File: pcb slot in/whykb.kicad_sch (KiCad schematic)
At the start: 89 parts, among them K1 KEYSW, K10 KEYSW, K11 KEYSW, K12 KEYSW, K13 KEYSW, K14 KEYSW, K15 KEYSW, K16 KEYSW, K17 KEYSW, K18 KEYSW, K19 KEYSW, K2 KEYSW, K20 KEYSW, K21 KEYSW, K22 KEYSW, K23 KEYSW, K24 KEYSW, K25 KEYSW, K26 KEYSW, K27 KEYSW, K28 KEYSW, K29 KEYSW, K3 KEYSW, K30 KEYSW, K31 KEYSW, K32 KEYSW, K33 KEYSW, K34 KEYSW, K35 KEYSW, K36 KEYSW, K37 KEYSW, K38 KEYSW, K39 KEYSW, K4 KEYSW, K40 KEYSW, K41 KEYSW, K42 KEYSW, K5 KEYSW, K6 KEYSW, K7 KEYSW, K8 KEYSW, K9 KEYSW, SW1 SW_PUSH, SW2 RotaryEncoder_Switch, U1 Elite-C, U2 SSD1306 128x32

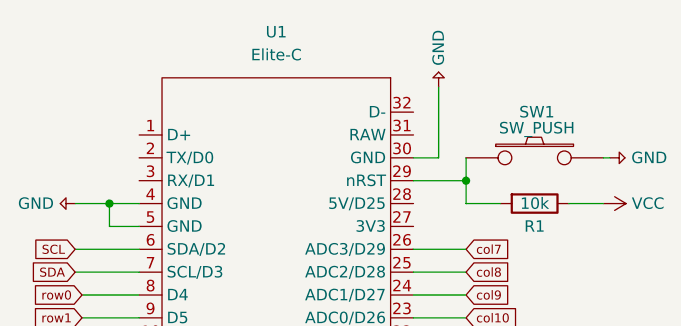
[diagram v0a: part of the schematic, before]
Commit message: made sea picro footprint
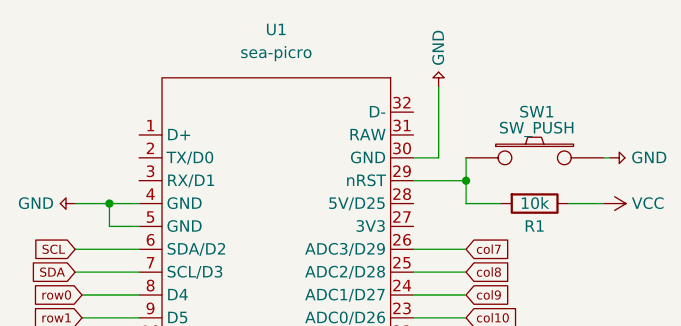
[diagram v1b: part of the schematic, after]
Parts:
- D1, D10, D11, D12, D13, D14, D15, D16, D17, D18, D19, D2, D20, D21, D22, D23, D24, D25, D26, D27, D28, D29, D3, D30, D31, D32, D33, D34, D35, D36, D37, D38, D39, D4, D40, D41, D42, D5, D6, D7, D8, D9: footprint (none) -> keyboard_parts:D_SOD123_axial
- K1, K12: footprint (none) -> keebs:Mx_Alps_150
- K10, K11, K14, K15, K16, K17, K18, K19, K2, K20, K21, K22, K24, K26, K27, K28, K29, K3, K30, K31, K32, K33, K34, K36, K37, K38, K39, K4, K42, K5, K6, K7, K8, K9: footprint (none) -> keebs:Mx_Alps_100
- K13: footprint (none) -> keebs:Mx_Alps_225
- K23, K25: footprint (none) -> keebs:Mx_Alps_175
- K35, K41: footprint (none) -> keebs:Mx_Alps_125
- K40: footprint (none) -> keebs:Mx_Alps_625
- R1: footprint (none) -> keebio_parts:R_0805
- SW1: footprint (none) -> Button_Switch_SMD:SW_SPST_TL3342
- SW2: footprint (none) -> keebio_parts:RotaryEncoder_Alps_EC11E-Switch_Vertical_H20mm
- U1: value Elite-C -> sea-picro; footprint (none) -> keebio_parts:Elite-C
- U2: footprint (none) -> KiCad-SSD1306-0.91-OLED-4pin-128x32:SSD1306-0.91-OLED-4pin-128x32

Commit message: start pcb layout
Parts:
- K1, K12: footprint keebs:Mx_Alps_150 -> MX_Only:MXOnly-1.5U-NoLED
- K10, K11, K14, K15, K16, K17, K18, K19, K2, K20, K21, K22, K24, K26, K27, K28, K29, K3, K30, K31, K32, K33, K34, K36, K37, K38, K39, K4, K42, K5, K6, K7, K8, K9: footprint keebs:Mx_Alps_100 -> MX_Only:MXOnly-1U-NoLED
- K13: footprint keebs:Mx_Alps_225 -> MX_Only:MXOnly-2.25U-NoLED
- K23, K25: footprint keebs:Mx_Alps_175 -> MX_Only:MXOnly-1.75U-NoLED
- K35, K41: footprint keebs:Mx_Alps_125 -> MX_Only:MXOnly-1.25U-NoLED
- K40: footprint keebs:Mx_Alps_625 -> MX_Only:MXOnly-7U-NoLED
- U1: footprint keebio_parts:Elite-C -> sea-picro:sea-picro

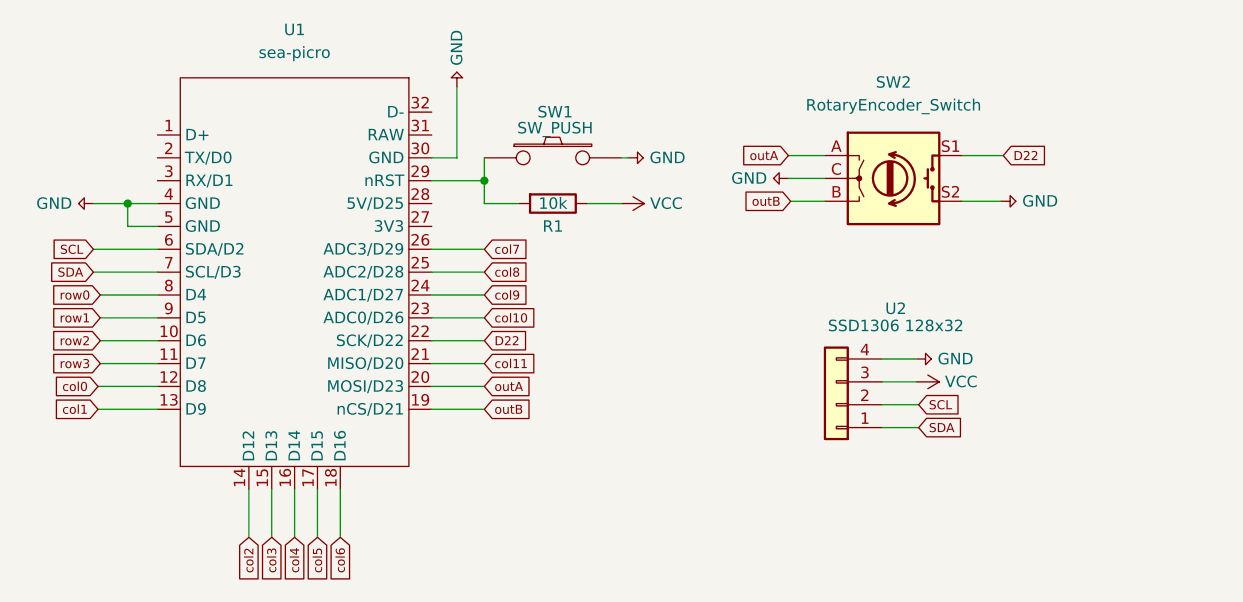
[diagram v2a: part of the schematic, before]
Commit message: routed traces
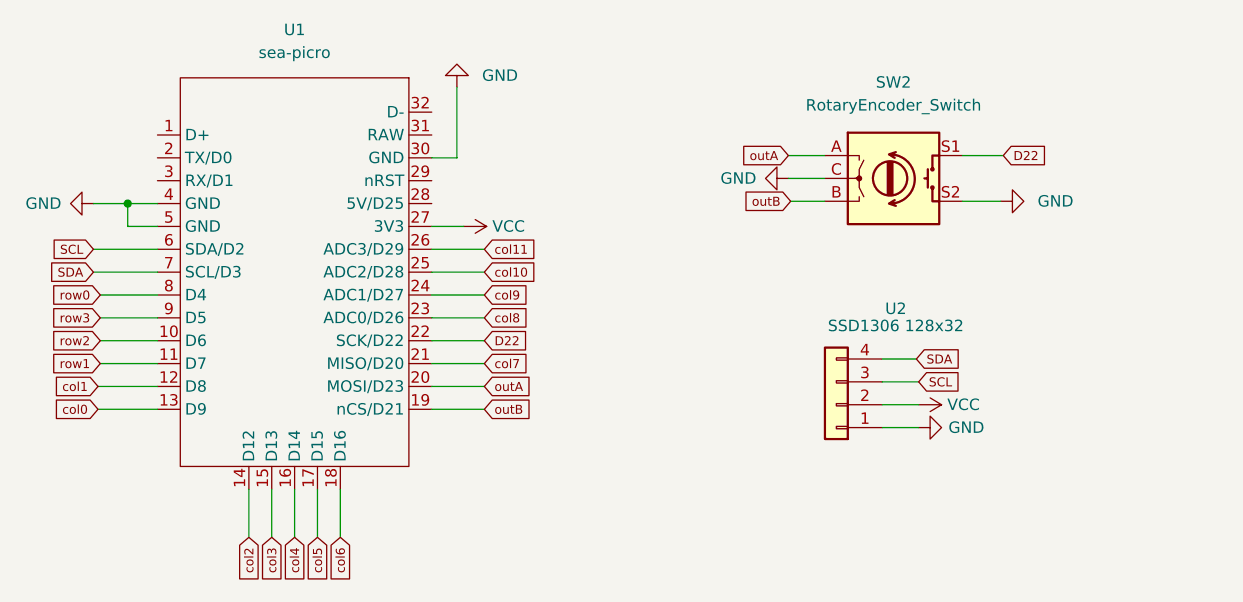
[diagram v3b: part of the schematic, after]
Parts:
- removed R1: 10k, keebio_parts:R_0805, symbol Device:R
- removed SW1: SW_PUSH, Button_Switch_SMD:SW_SPST_TL3342, symbol keyboard_parts:SW_PUSH
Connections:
- net SCL: now also U2.3 (Pin_3); no longer U2.2 (Pin_2)
- net SDA: now also U2.4 (Pin_4); no longer U2.1 (Pin_1)
- net VCC: now also U1.27 (3V3), U2.2 (Pin_2); no longer U2.3 (Pin_3)
- net col0: now also U1.13 (D9); no longer U1.12 (D8)
- net col1: now also U1.12 (D8); no longer U1.13 (D9)
- net col10: now also U1.25 (ADC2/D28); no longer U1.23 (ADC0/D26)
- net col11: now also U1.26 (ADC3/D29); no longer U1.21 (MISO/D20)
- net col7: now also U1.21 (MISO/D20); no longer U1.26 (ADC3/D29)
- net col8: now also U1.23 (ADC0/D26); no longer U1.25 (ADC2/D28)
- net row1: now also U1.11 (D7); no longer U1.9 (D5)
- net row3: now also U1.9 (D5); no longer U1.11 (D7)
- net +5V renamed GND
- net GND: now also U2.1 (Pin_1); no longer U2.4 (Pin_4)

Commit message: update pcb
cleaned up traces
added some silkscreen
generate gerbers
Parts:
- D1, D10, D11, D12, D13, D14, D15, D16, D17, D18, D19, D2, D20, D21, D22, D23, D24, D25, D26, D27, D28, D29, D3, D30, D31, D32, D33, D34, D35, D36, D37, D38, D39, D4, D40, D41, D42, D5, D6, D7, D8, D9: footprint keyboard_parts:D_SOD123_axial -> keyboard_parts:D_SOD123
